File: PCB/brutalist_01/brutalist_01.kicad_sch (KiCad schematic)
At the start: 53 parts, among them U0 CD74HC4067M, U1 CD74HC4067M, U2 CD74HC4067M, U3 CD74HC4067M

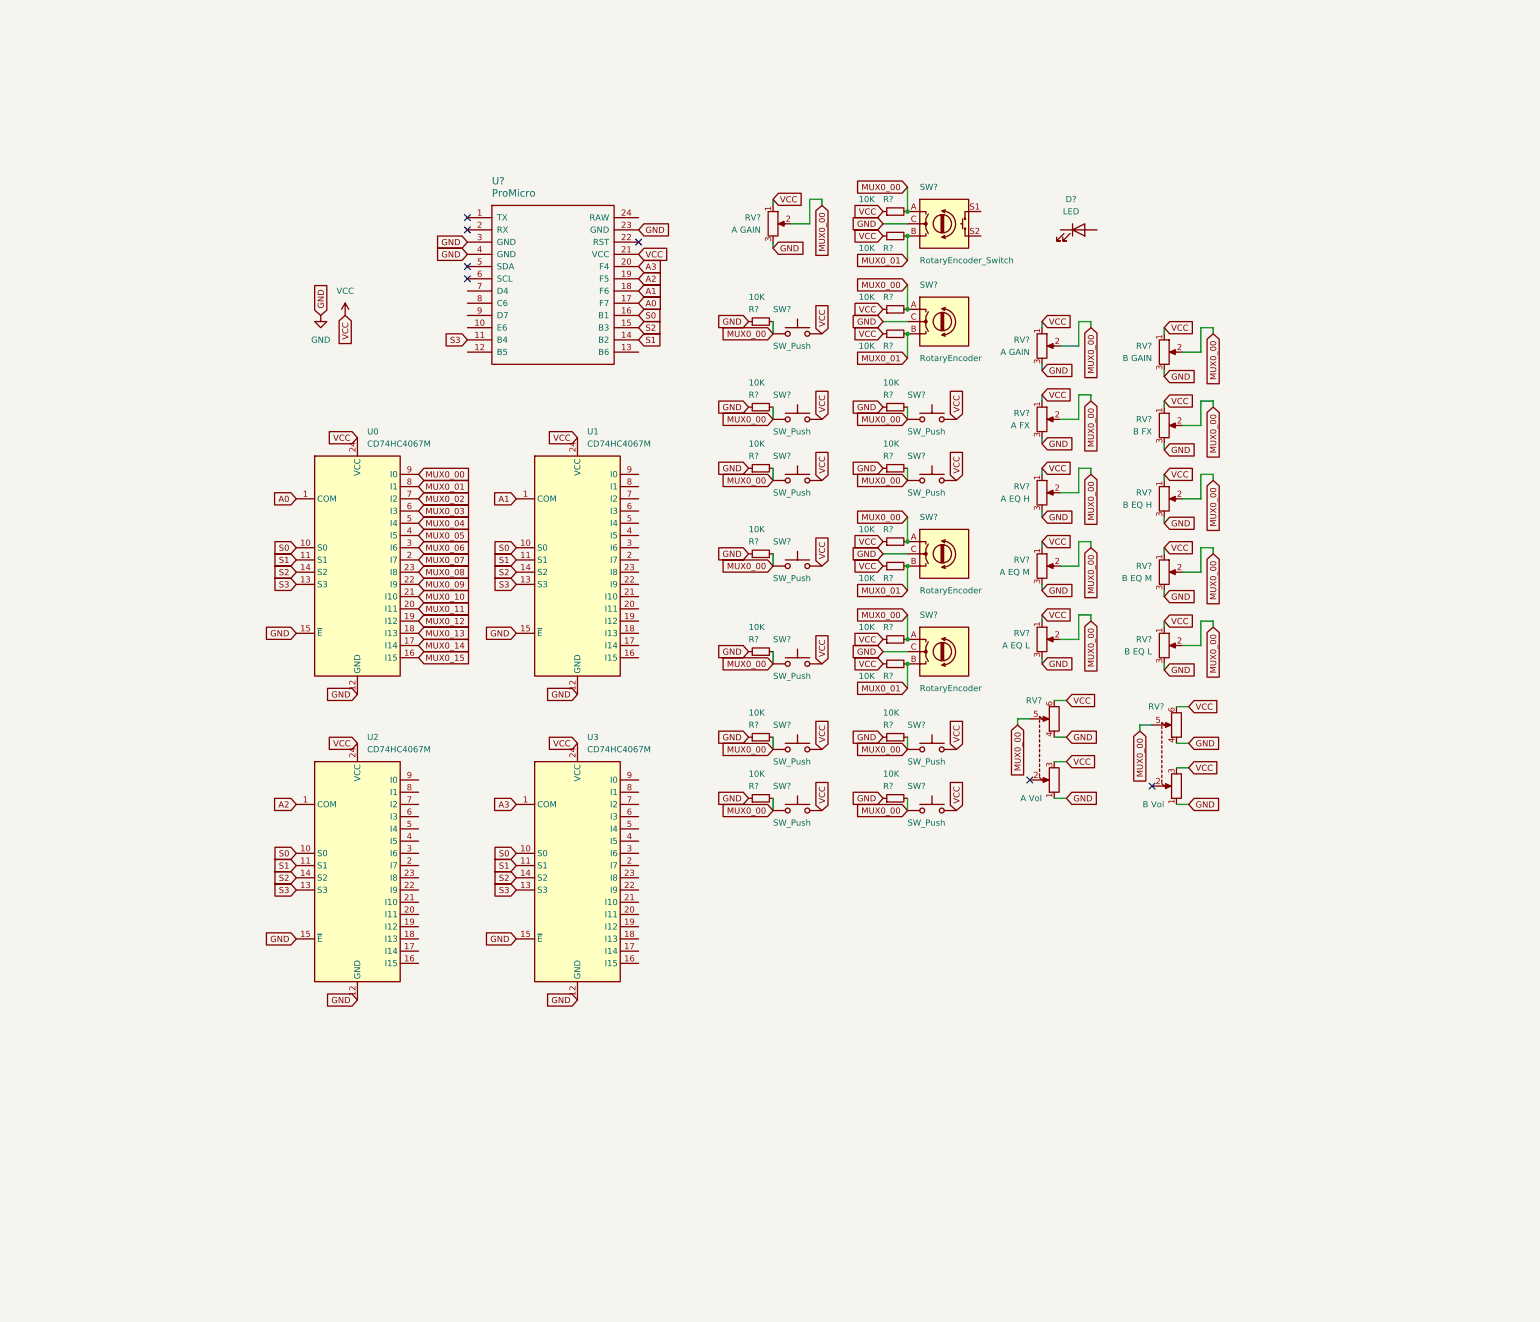
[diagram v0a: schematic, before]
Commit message: update schematic to nano
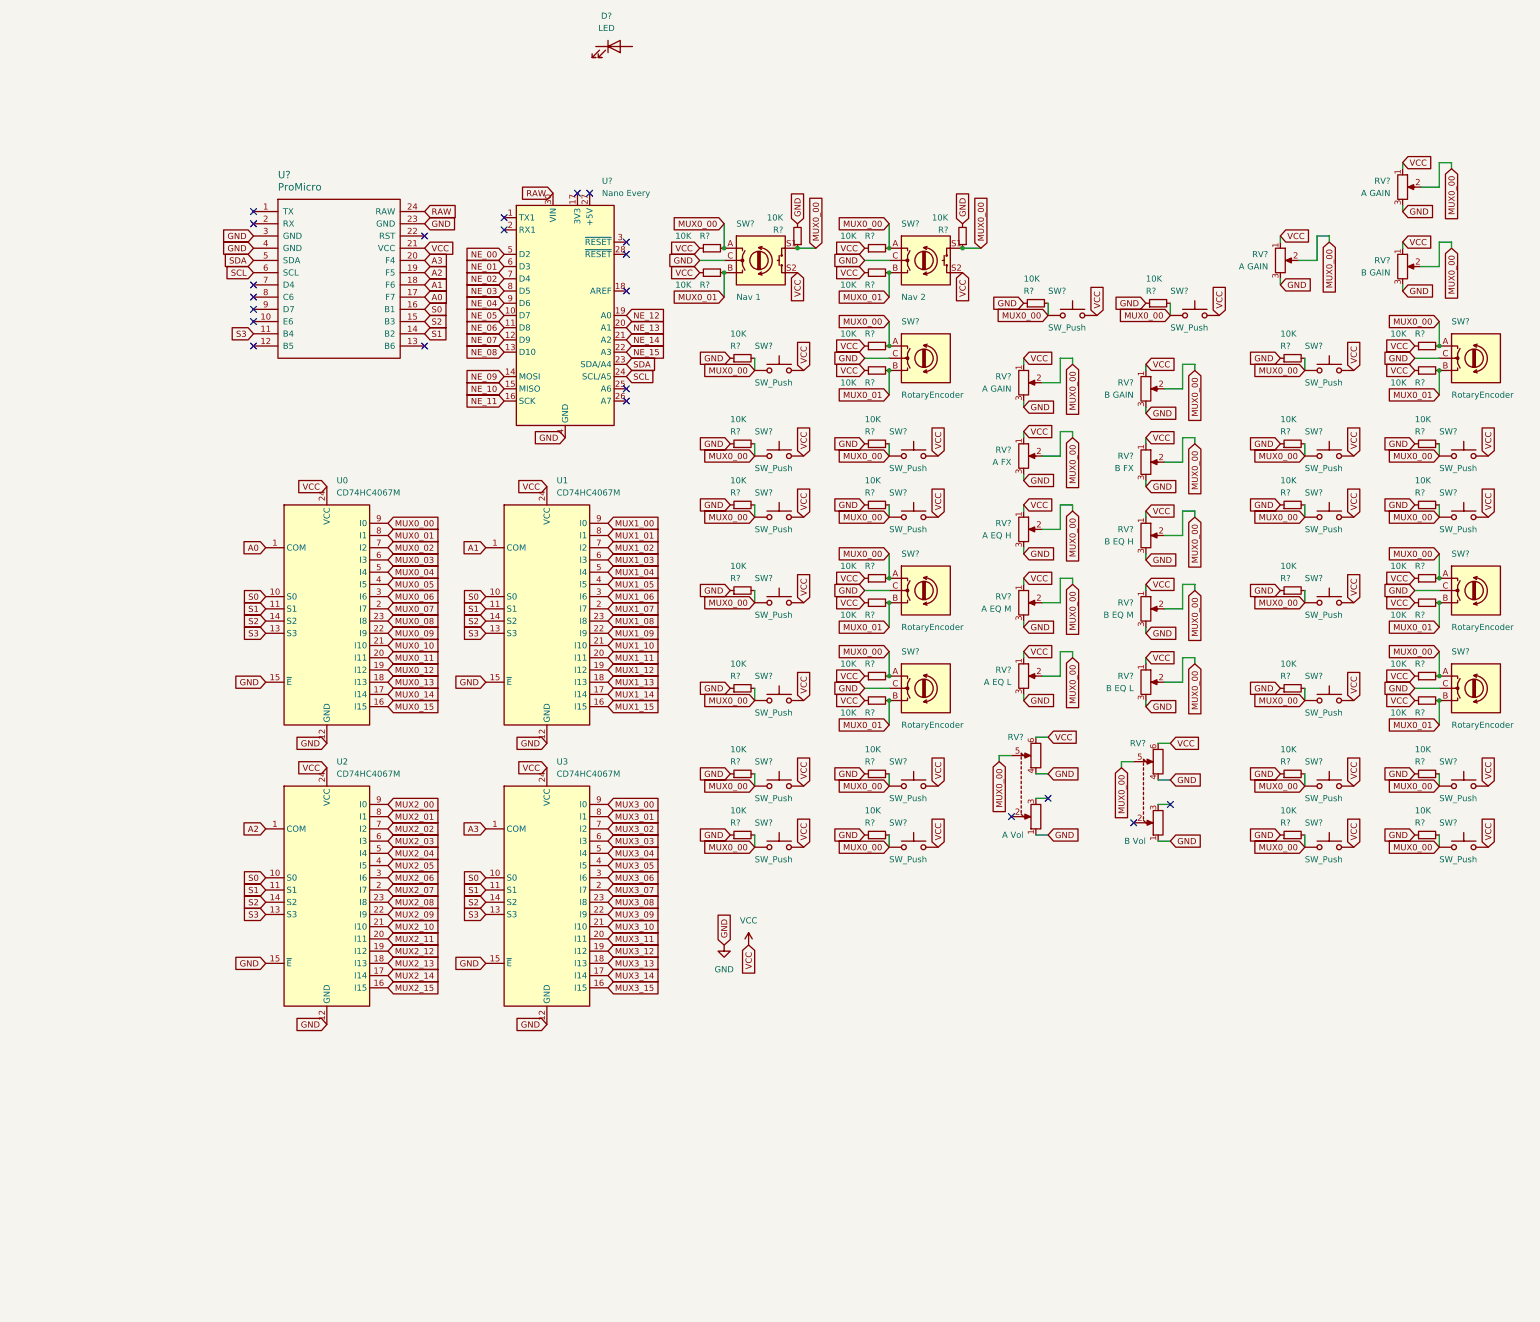
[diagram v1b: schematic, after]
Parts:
- added R? (x23): 10K, symbol Device:R_Small
- added RV?: B GAIN, symbol Device:R_Potentiometer
- added RV?: A GAIN, symbol Device:R_Potentiometer
- added SW? (x13): SW_Push, symbol Switch:SW_Push
- added SW? (x3): RotaryEncoder, symbol Device:RotaryEncoder
- added SW?: Nav 1, symbol Device:RotaryEncoder_Switch
- added U?: Nano Every, Module:Arduino_Nano, symbol MCU_Module:Arduino_Nano_Every
- SW?: value RotaryEncoder_Switch -> Nav 2
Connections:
- net GND: now also R?.1, R?.1, R?.1, R?.1, R?.1, R?.1, R?.1, R?.1, R?.1, R?.1, R?.1, R?.1, R?.1, R?.2, R?.2, RV?.3, RV?.3, SW?.C, SW?.C, SW?.C, SW?.C, U?.29 (GND), U?.4 (GND)
- net MUX0_00: now also SW?.S1, R?.1, R?.1, R?.2, R?.2, R?.2, R?.2, R?.2, R?.2, R?.2, R?.2, R?.2, R?.2, R?.2, R?.2, R?.2, R?.2, R?.2, R?.2, R?.2, RV?.2, RV?.2, SW?.1, SW?.1, SW?.1, SW?.1, SW?.1, SW?.1, SW?.1, SW?.1, SW?.1, SW?.1, SW?.1, SW?.1, SW?.1, SW?.A, SW?.A, SW?.A, SW?.A, SW?.S1
- net MUX0_01: now also R?.2, R?.2, R?.2, R?.2, SW?.B, SW?.B, SW?.B, SW?.B
- net VCC: now also SW?.S2, R?.1, R?.1, R?.1, R?.1, R?.1, R?.1, R?.1, R?.1, RV?.1, RV?.1, SW?.2, SW?.2, SW?.2, SW?.2, SW?.2, SW?.2, SW?.2, SW?.2, SW?.2, SW?.2, SW?.2, SW?.2, SW?.2, SW?.S2; no longer RV?.3, RV?.3
- net RAW: now reaches U?.24 (RAW)
- net RAW: now also U?.30 (VIN)
- net SDA: now reaches U?.5 (SDA)
- net SDA: now also U?.23 (SDA/A4)
- net SCL: now reaches U?.6 (SCL)
- net SCL: now also U?.24 (SCL/A5)
- net MUX3_15: now reaches U3.16 (I15)
- net MUX3_14: now reaches U3.17 (I14)
- net MUX3_13: now reaches U3.18 (I13)
- net MUX3_12: now reaches U3.19 (I12)
- net MUX3_07: now reaches U3.2 (I7)
- net MUX3_11: now reaches U3.20 (I11)
- net MUX3_10: now reaches U3.21 (I10)
- net MUX3_09: now reaches U3.22 (I9)
- net MUX3_08: now reaches U3.23 (I8)
- net MUX3_06: now reaches U3.3 (I6)
- net MUX3_05: now reaches U3.4 (I5)
- net MUX3_04: now reaches U3.5 (I4)
- net MUX3_03: now reaches U3.6 (I3)
- net MUX3_02: now reaches U3.7 (I2)
- net MUX3_01: now reaches U3.8 (I1)
- net MUX3_00: now reaches U3.9 (I0)
- net MUX2_15: now reaches U2.16 (I15)
- net MUX2_14: now reaches U2.17 (I14)
- net MUX2_13: now reaches U2.18 (I13)
- net MUX2_12: now reaches U2.19 (I12)
- net MUX2_07: now reaches U2.2 (I7)
- net MUX2_11: now reaches U2.20 (I11)
- net MUX2_10: now reaches U2.21 (I10)
- net MUX2_09: now reaches U2.22 (I9)
- net MUX2_08: now reaches U2.23 (I8)
- net MUX2_06: now reaches U2.3 (I6)
- net MUX2_05: now reaches U2.4 (I5)
- net MUX2_04: now reaches U2.5 (I4)
- net MUX2_03: now reaches U2.6 (I3)
- net MUX2_02: now reaches U2.7 (I2)
- net MUX2_01: now reaches U2.8 (I1)
- net MUX2_00: now reaches U2.9 (I0)
- net MUX1_15: now reaches U1.16 (I15)
- net MUX1_14: now reaches U1.17 (I14)
- net MUX1_13: now reaches U1.18 (I13)
- net MUX1_12: now reaches U1.19 (I12)
- net MUX1_07: now reaches U1.2 (I7)
- net MUX1_11: now reaches U1.20 (I11)
- net MUX1_10: now reaches U1.21 (I10)
- net MUX1_09: now reaches U1.22 (I9)
- net MUX1_08: now reaches U1.23 (I8)
- net MUX1_06: now reaches U1.3 (I6)
- net MUX1_05: now reaches U1.4 (I5)
- net MUX1_04: now reaches U1.5 (I4)
- net MUX1_03: now reaches U1.6 (I3)
- net MUX1_02: now reaches U1.7 (I2)
- net MUX1_01: now reaches U1.8 (I1)
- net MUX1_00: now reaches U1.9 (I0)
- new net NE_00: U?.5 (D2)
- new net NE_01: U?.6 (D3)
- new net NE_02: U?.7 (D4)
- new net NE_03: U?.8 (D5)
- new net NE_04: U?.9 (D6)
- new net NE_05: U?.10 (D7)
- new net NE_06: U?.11 (D8)
- new net NE_07: U?.12 (D9)
- new net NE_08: U?.13 (D10)
- new net NE_09: U?.14 (MOSI)
- new net NE_10: U?.15 (MISO)
- new net NE_11: U?.16 (SCK)
- new net NE_12: U?.19 (A0)
- new net NE_13: U?.20 (A1)
- new net NE_14: U?.21 (A2)
- new net NE_15: U?.22 (A3)
- no-connect marks 7 -> 22
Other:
- company: (none) -> BSPLT
- title: (none) -> Brutalist Midi Mixer
- moved on the sheet: D?, R?, RV?, SW?, U0, U1, U2, U3, U?

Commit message: update schematic
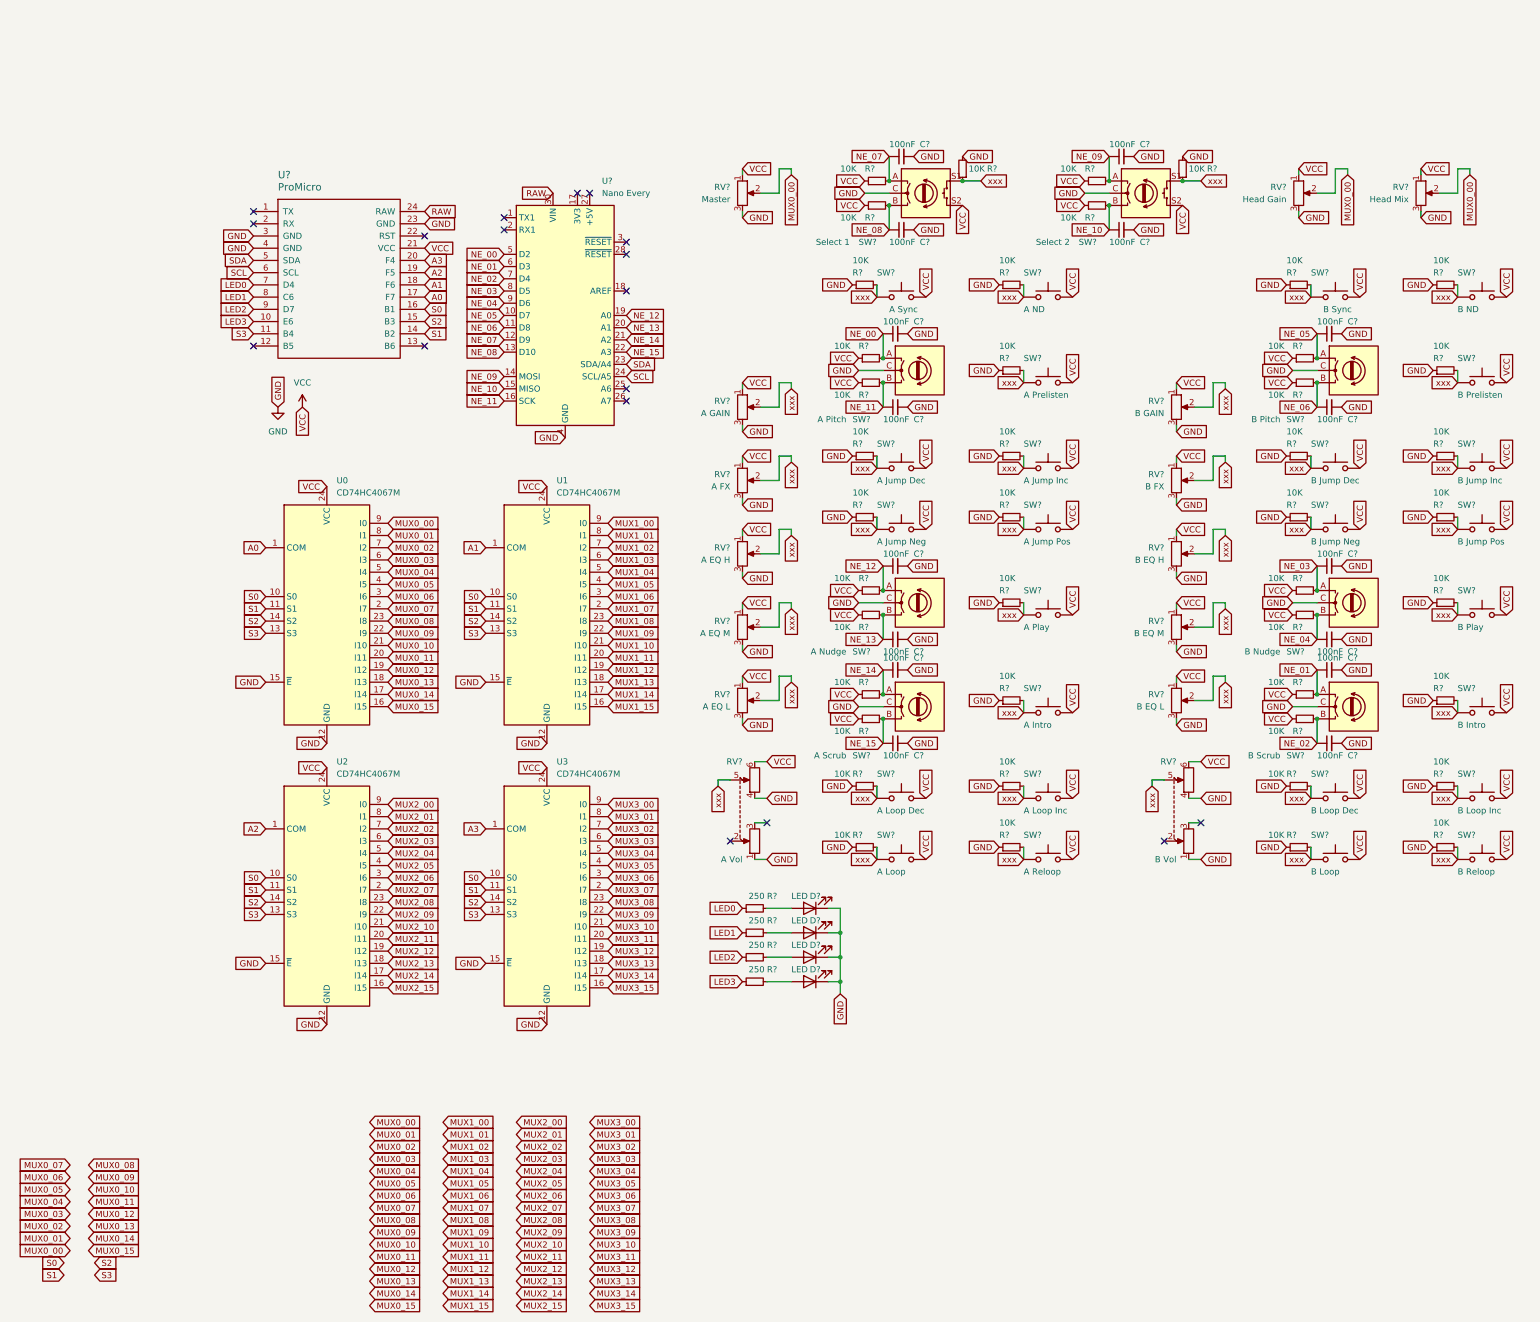
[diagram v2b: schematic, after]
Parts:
- removed R? (x28): 10K, symbol Device:R_Small
- removed RV?: B GAIN, symbol Device:R_Potentiometer
- removed RV?: B EQ H, symbol Device:R_Potentiometer
- removed RV?: B EQ L, symbol Device:R_Potentiometer
- removed RV?: B Vol, symbol Device:R_Potentiometer_Dual
- removed RV?: B FX, symbol Device:R_Potentiometer
- removed RV?: B EQ M, symbol Device:R_Potentiometer
- removed SW? (x13): SW_Push, symbol Switch:SW_Push
- removed SW? (x6): RotaryEncoder, symbol Device:RotaryEncoder
- removed SW?: Nav 2, symbol Device:RotaryEncoder_Switch
- added C? (x16): 100nF, symbol Device:C_Small
- added D? (x3): LED, symbol Device:LED
- added R? (x30): 10K, symbol Device:R_Small
- added R? (x4): 250, symbol Device:R_Small
- added RV?: B GAIN, symbol Device:R_Potentiometer
- added RV?: B FX, symbol Device:R_Potentiometer
- added RV?: B EQ H, symbol Device:R_Potentiometer
- added RV?: B EQ L, symbol Device:R_Potentiometer
- added RV?: B Vol, symbol Device:R_Potentiometer_Dual
- added RV?: B EQ M, symbol Device:R_Potentiometer
- added SW?: B Nudge, symbol Device:RotaryEncoder
- added SW?: B Jump Dec, symbol Switch:SW_Push
- added SW?: B Play, symbol Switch:SW_Push
- added SW?: Select 2, symbol Device:RotaryEncoder_Switch
- added SW?: B Loop, symbol Switch:SW_Push
- added SW?: A Sync, symbol Switch:SW_Push
- added SW?: A ND, symbol Switch:SW_Push
- added SW?: B Jump Pos, symbol Switch:SW_Push
- added SW?: B Intro, symbol Switch:SW_Push
- added SW?: A Scrub, symbol Device:RotaryEncoder
- added SW?: B Loop Inc, symbol Switch:SW_Push
- added SW?: A Nudge, symbol Device:RotaryEncoder
- added SW?: B Scrub, symbol Device:RotaryEncoder
- added SW?: B Jump Inc, symbol Switch:SW_Push
- added SW?: B Loop Dec, symbol Switch:SW_Push
- added SW?: B ND, symbol Switch:SW_Push
- added SW?: A Pitch, symbol Device:RotaryEncoder
- added SW?: B Reloop, symbol Switch:SW_Push
- added SW?: B Jump Neg, symbol Switch:SW_Push
- added SW?: B Prelisten, symbol Switch:SW_Push
- added SW?: B Sync, symbol Switch:SW_Push
- added SW?: B Pitch, symbol Device:RotaryEncoder
- RV?: value A GAIN -> Master
- RV?: value B GAIN -> Head Mix
- RV?: value A GAIN -> Head Gain
- SW?: value SW_Push -> A Loop Dec
- SW?: value SW_Push -> A Jump Pos
- SW?: value SW_Push -> A Jump Dec
- SW?: value Nav 1 -> Select 1
- SW?: value SW_Push -> A Jump Inc
- SW?: value SW_Push -> A Loop Inc
- SW?: value SW_Push -> A Prelisten
- SW?: value SW_Push -> A Loop
- SW?: value SW_Push -> A Intro
- SW?: value SW_Push -> A Jump Neg
- SW?: value SW_Push -> A Reloop
- SW?: value SW_Push -> A Play
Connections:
- net GND: now also D?.1 (K), C?.2, C?.2, C?.2, C?.2, C?.2, C?.2, C?.2, C?.2, C?.2, C?.2, C?.2, C?.2, C?.2, C?.2, C?.2, C?.2, D?.1 (K), D?.1 (K), D?.1 (K), R?.1, R?.1, R?.1, R?.1, R?.1, R?.1, R?.1, R?.1, R?.1, R?.1, R?.1, R?.1, R?.1, R?.1, R?.1, R?.2, RV?.1, RV?.3, RV?.3, RV?.3, RV?.3, RV?.3, RV?.4, SW?.C, SW?.C, SW?.C, SW?.C, SW?.C, SW?.C, SW?.C
- net MUX0_00: no longer R?.1, R?.2, R?.2, R?.2, R?.2, R?.2, R?.2, R?.2, R?.2, R?.2, R?.2, R?.2, R?.2, RV?.2, RV?.2, RV?.2, RV?.2, RV?.2, RV?.5, SW?.1, SW?.1, SW?.1, SW?.1, SW?.1, SW?.1, SW?.1, SW?.1, SW?.1, SW?.1, SW?.1, SW?.A, SW?.S1
- net MUX0_01: no longer R?.2, SW?.B
- net NE_00: now also C?.1, R?.2, SW?.A
- net NE_01: now also C?.1, R?.2, SW?.A
- net NE_02: now also C?.1, R?.2, SW?.B
- net NE_03: now also C?.1, R?.2, SW?.A
- net NE_04: now also C?.1, R?.2, SW?.B
- net NE_05: now also C?.1, R?.2, SW?.A
- net NE_06: now also C?.1, R?.2, SW?.B
- net NE_07: now also R?.2, SW?.A, C?.1
- net NE_08: now also R?.2, SW?.B, C?.1
- net NE_09: now also C?.1, R?.2, SW?.A
- net NE_10: now also C?.1, R?.2, SW?.B
- net NE_11: now also C?.1, R?.2, SW?.B
- net NE_12: now also C?.1, R?.2, SW?.A
- net NE_13: now also C?.1, R?.2, SW?.B
- net NE_14: now also C?.1, R?.2, SW?.A
- net NE_15: now also C?.1, R?.2, SW?.B
- net VCC: now also R?.1, R?.1, R?.1, R?.1, R?.1, R?.1, R?.1, R?.1, R?.1, R?.1, R?.1, R?.1, R?.1, R?.1, RV?.1, RV?.1, RV?.1, RV?.1, RV?.1, RV?.6, SW?.2, SW?.2, SW?.2, SW?.2, SW?.2, SW?.2, SW?.2, SW?.2, SW?.2, SW?.2, SW?.2, SW?.2, SW?.2, SW?.2, SW?.2, SW?.S2
- net LED3: now reaches U?.10 (E6)
- net LED3: now also R?.1
- net LED0: now reaches U?.7 (D4)
- net LED0: now also R?.1
- net LED1: now reaches U?.8 (C6)
- net LED1: now also R?.1
- net LED2: now reaches U?.9 (D7)
- net LED2: now also R?.1
- net at D?.2 (A): now also R?.2
- new net: D?.2 (A), R?.2 (x3)
- new net xxx: R?.1, R?.1, R?.2, R?.2, R?.2, R?.2, R?.2, R?.2, R?.2, R?.2, R?.2, R?.2, R?.2, R?.2, R?.2, R?.2, R?.2, R?.2, R?.2, R?.2, R?.2, R?.2, R?.2, R?.2, R?.2, R?.2, R?.2, R?.2, RV?.2, RV?.2, RV?.2, RV?.2, RV?.2, RV?.2, RV?.2, RV?.2, RV?.2, RV?.2, RV?.5, RV?.5, SW?.1, SW?.1, SW?.1, SW?.1, SW?.1, SW?.1, SW?.1, SW?.1, SW?.1, SW?.1, SW?.1, SW?.1, SW?.1, SW?.1, SW?.1, SW?.1, SW?.1, SW?.1, SW?.1, SW?.1, SW?.1, SW?.1, SW?.1, SW?.1, SW?.1, SW?.1, SW?.S1, SW?.S1
- no-connect marks 22 -> 18
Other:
- moved on the sheet: D?, R?, RV?, SW?

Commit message: update schematic
maybe finished
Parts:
- gave numbers to parts that had none: 119
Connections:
- net MUX0_00: now also R7.2, SW3.1; no longer RV1.2, RV14.2, RV15.2
- net MUX0_01: now also R6.2, SW2.1
- net MUX0_02: now also R5.2, SW1.1
- net MUX0_03: now also R19.2, SW10.1
- net MUX0_04: now also R20.2, SW11.1
- net MUX0_05: now also R21.2, SW12.1
- net MUX0_06: now also R22.2, SW13.1
- net MUX0_08: now also R23.2, SW14.1
- net MUX0_09: now also R24.2, SW15.1
- net MUX0_10: now also R25.2, SW16.1
- net MUX0_11: now also R26.2, SW17.1
- net MUX0_12: now also R9.2, SW5.1
- net MUX0_13: now also R8.2, SW4.1
- net MUX1_00: now also R32.2, SW21.1
- net MUX1_01: now also R31.2, SW20.1
- net MUX1_02: now also R30.2, SW19.1
- net MUX1_03: now also R41.2, SW27.1
- net MUX1_04: now also R42.2, SW28.1
- net MUX1_05: now also R43.2, SW29.1
- net MUX1_06: now also R44.2, SW30.1
- net MUX1_08: now also R45.2, SW31.1
- net MUX1_09: now also R46.2, SW32.1
- net MUX1_10: now also R47.2, SW33.1
- net MUX1_11: now also R48.2, SW34.1
- net MUX1_12: now also R34.2, SW23.1
- net MUX1_13: now also R33.2, SW22.1
- net MUX2_00: now also RV6.2
- net MUX2_01: now also RV5.2
- net MUX2_02: now also RV4.2
- net MUX2_03: now also RV3.2
- net MUX2_04: now also RV2.2
- net MUX2_05: now also RV1.2
- net MUX2_13: now also RV7.5
- net MUX3_00: now also RV12.2
- net MUX3_01: now also RV11.2
- net MUX3_02: now also RV10.2
- net MUX3_03: now also RV9.2
- net MUX3_04: now also RV8.2
- net MUX3_05: now also RV14.2
- net MUX3_06: now also RV15.2
- net MUX3_13: now also RV13.5
- net xxx: no longer R19.2, R20.2, R21.2, R22.2, R23.2, R24.2, R25.2, R26.2, R30.2, R31.2, R32.2, R33.2, R34.2, R41.2, R42.2, R43.2, R44.2, R45.2, R46.2, R47.2, R48.2, R5.2, R6.2, R7.2, R8.2, R9.2, RV10.2, RV11.2, RV12.2, RV13.5, RV2.2, RV3.2, RV4.2, RV5.2, RV6.2, RV7.5, RV8.2, RV9.2, SW1.1, SW10.1, SW11.1, SW12.1, SW13.1, SW14.1, SW15.1, SW16.1, SW17.1, SW19.1, SW2.1, SW20.1, SW21.1, SW22.1, SW23.1, SW27.1, SW28.1, SW29.1, SW3.1, SW30.1, SW31.1, SW32.1, SW33.1, SW34.1, SW4.1, SW5.1
- no-connect marks 18 -> 41
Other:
- moved on the sheet: D1, D2, D3, D4, R1, R2, R3, R4
